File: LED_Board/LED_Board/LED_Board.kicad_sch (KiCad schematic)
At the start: 2 parts, among them J1 Conn_01x02

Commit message: Made preliminary footprint for WHITE LED!
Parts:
- D1: footprint (none) -> AF_Footprint:CUN06B1B
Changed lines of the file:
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@@
 			)
 		)
-		(property "Footprint" ""
+		(property "Footprint" "AF_Footprint:CUN06B1B"
 			(at 132.08 82.55 0)
 			(hide yes)

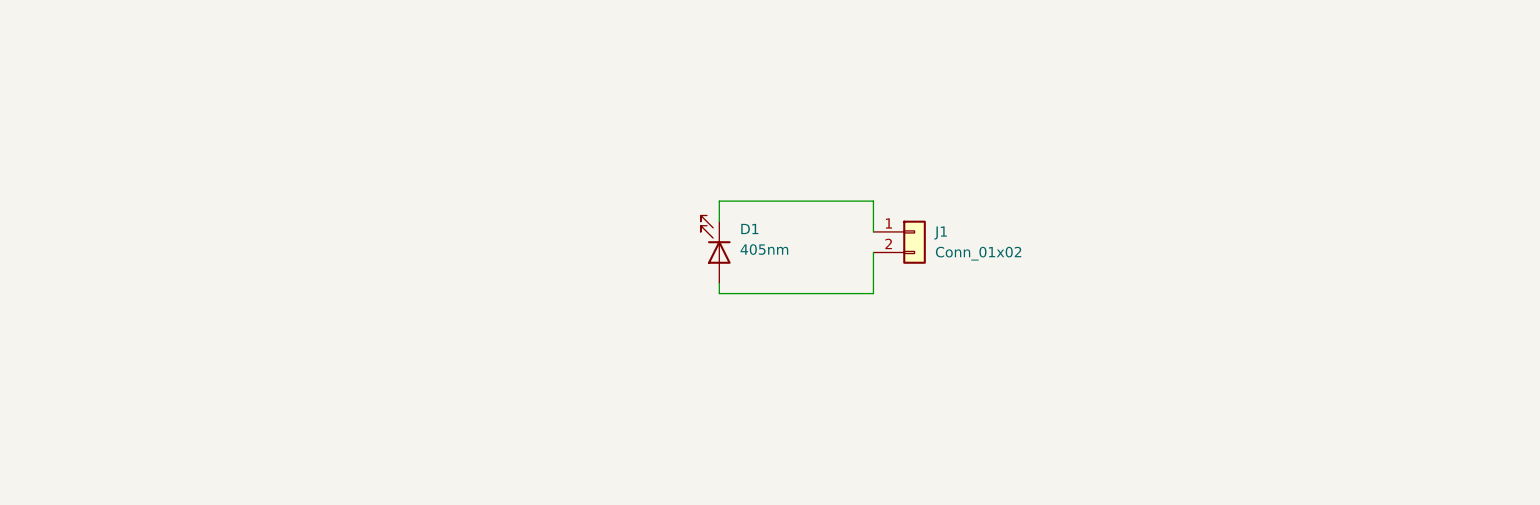
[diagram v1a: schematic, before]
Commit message: Fixed up schematic, some footprints still need fixing
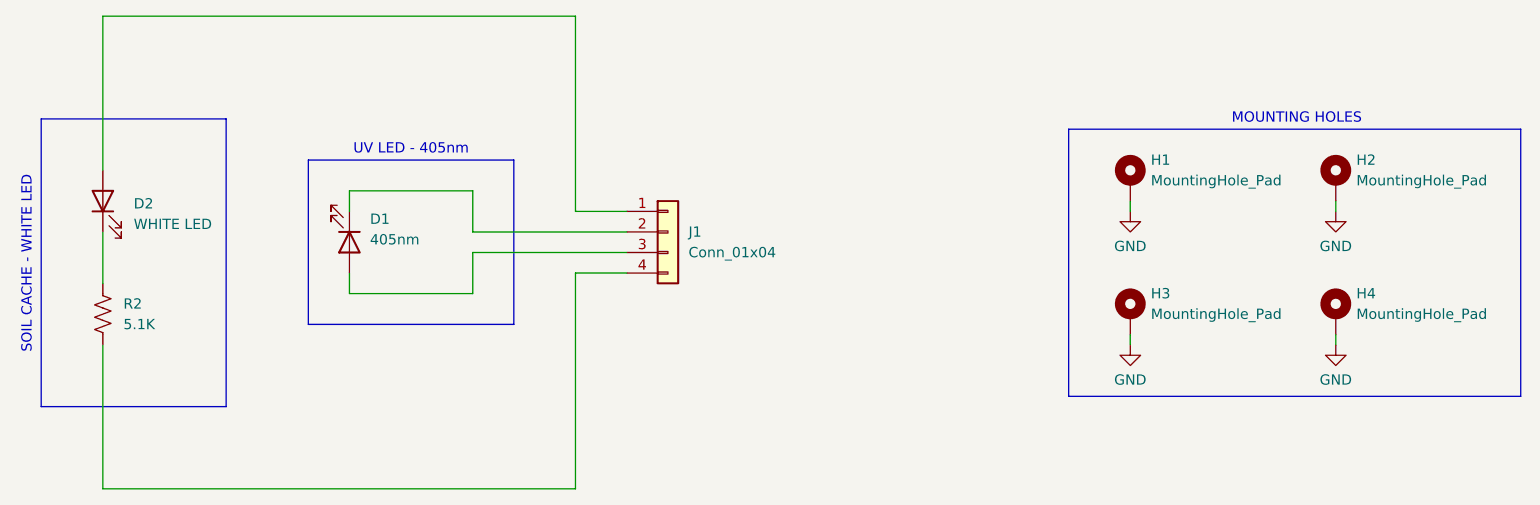
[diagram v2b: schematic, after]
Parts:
- removed J1: Conn_01x02, symbol Connector_Generic:Conn_01x02
- added D2: WHITE LED, Diode_SMD:D_0603_1608Metric_Pad1.05x0.95mm_HandSolder, symbol Device:LED
- added H1, H2, H3, H4: MountingHole_Pad, MRDT_Drill_Holes:4_40_Hole_Pad_Via, symbol Mechanical:MountingHole_Pad
- added J1: Conn_01x04, Connector_JST:JST_PH_S4B-PH-K_1x04_P2.00mm_Horizontal, symbol Connector_Generic:Conn_01x04
- added R2: 5.1K, Resistor_SMD:R_0603_1608Metric_Pad0.98x0.95mm_HandSolder, symbol Device:R_US
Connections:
- net at D1.1 (K): now also J1.2 (Pin_2)
- net at D1.2 (A): now also J1.3 (Pin_3)
- new net: D2.1 (K), R2.1
- new net: D2.2 (A), J1.1 (Pin_1)
- new net: J1.4 (Pin_4), R2.2
- new net GND: H1.1, H2.1, H3.1, H4.1
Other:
- note added: "MOUNTING HOLES"
- note added: "SOIL CACHE - WHITE LED"
- note added: "UV LED - 405nm"
- moved on the sheet: D1

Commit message: Add footprint
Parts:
- J1: footprint Connector_JST:JST_PH_S4B-PH-K_1x04_P2.00mm_Horizontal -> Connector_JST:JST_PH_B4B-PH-SM4-TB_1x04-1MP_P2.00mm_Vertical
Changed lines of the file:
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@@
 			)
 		)
-		(property "Footprint" "Connector_JST:JST_PH_S4B-PH-K_1x04_P2.00mm_Horizontal"
+		(property "Footprint" "Connector_JST:JST_PH_B4B-PH-SM4-TB_1x04-1MP_P2.00mm_Vertical"
 			(at 125.73 80.01 0)
 			(hide yes)

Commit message: Finalized Initial Layout
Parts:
- J1: footprint Connector_JST:JST_PH_B4B-PH-SM4-TB_1x04-1MP_P2.00mm_Vertical -> Connector_JST:JST_PH_S4B-PH-SM4-TB_1x04-1MP_P2.00mm_Horizontal
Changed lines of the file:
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@@
 			)
 		)
-		(property "Footprint" "Connector_JST:JST_PH_B4B-PH-SM4-TB_1x04-1MP_P2.00mm_Vertical"
+		(property "Footprint" "Connector_JST:JST_PH_S4B-PH-SM4-TB_1x04-1MP_P2.00mm_Horizontal"
 			(at 125.73 80.01 0)
 			(hide yes)
